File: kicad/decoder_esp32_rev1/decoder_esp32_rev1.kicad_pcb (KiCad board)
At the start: 2 copper layers, 75.9 x 42 mm, 53 parts, among them J1 TRCK_IN, J2 F_2, J3 F_3, J4 F_1, J5 F_4, J6 AUX_5V, J8 MTR_OUT, J9 to_cap_brd, Q1 BSS138, Q2 BSS138, Q3 BSS138, Q4 BSS138, U1 ESP32-C3_SUPERMINI_TH, U2 LM2596S-5, U3 TB67H450FNG_EL

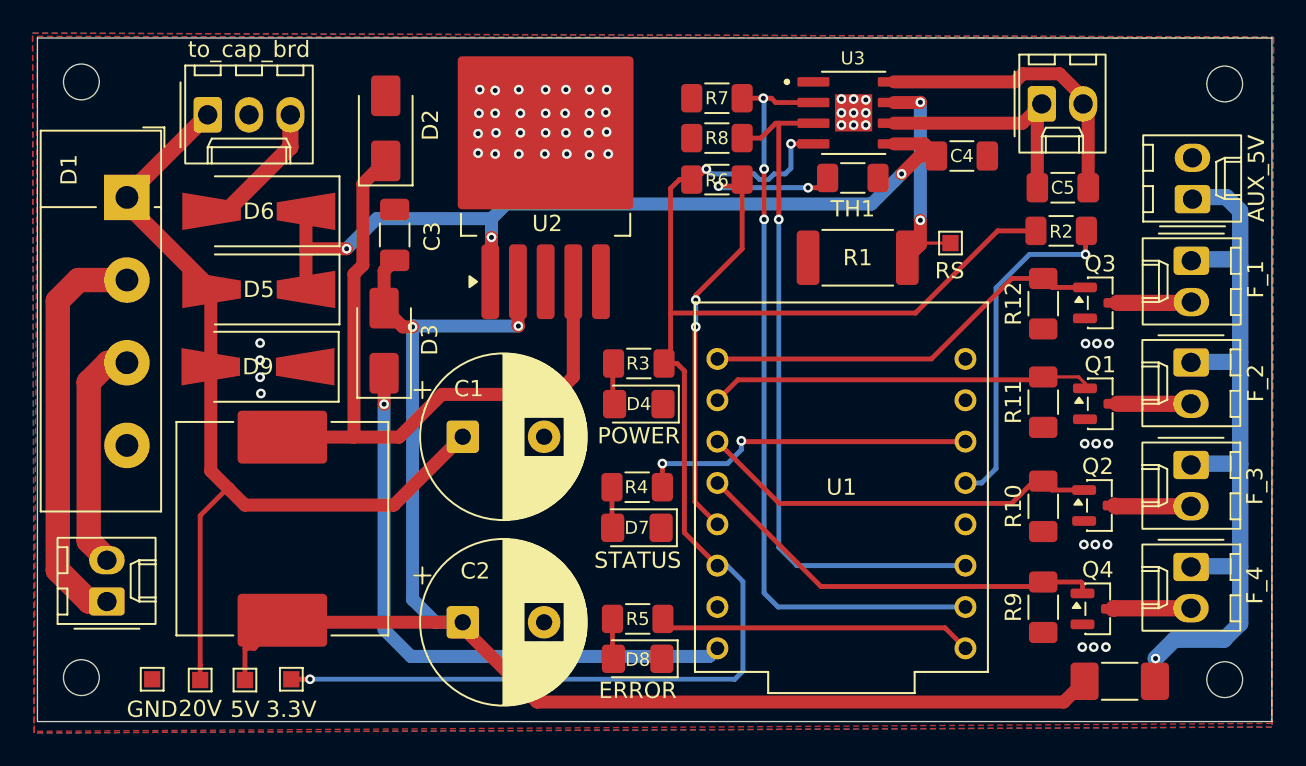
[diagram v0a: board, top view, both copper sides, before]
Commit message: KiCad rev3: schematic/PCB layout reorganization + remove PWR_FLAG symbols
Reordered components and wiring for better schematic overview.
Removed #FLG01/#FLG02 PWR_FLAG symbols (cosmetic ERC cleanup).
No netlist or component value changes.

Co-Authored-By: Claude Sonnet 4.6 <noreply@anthropic.com>
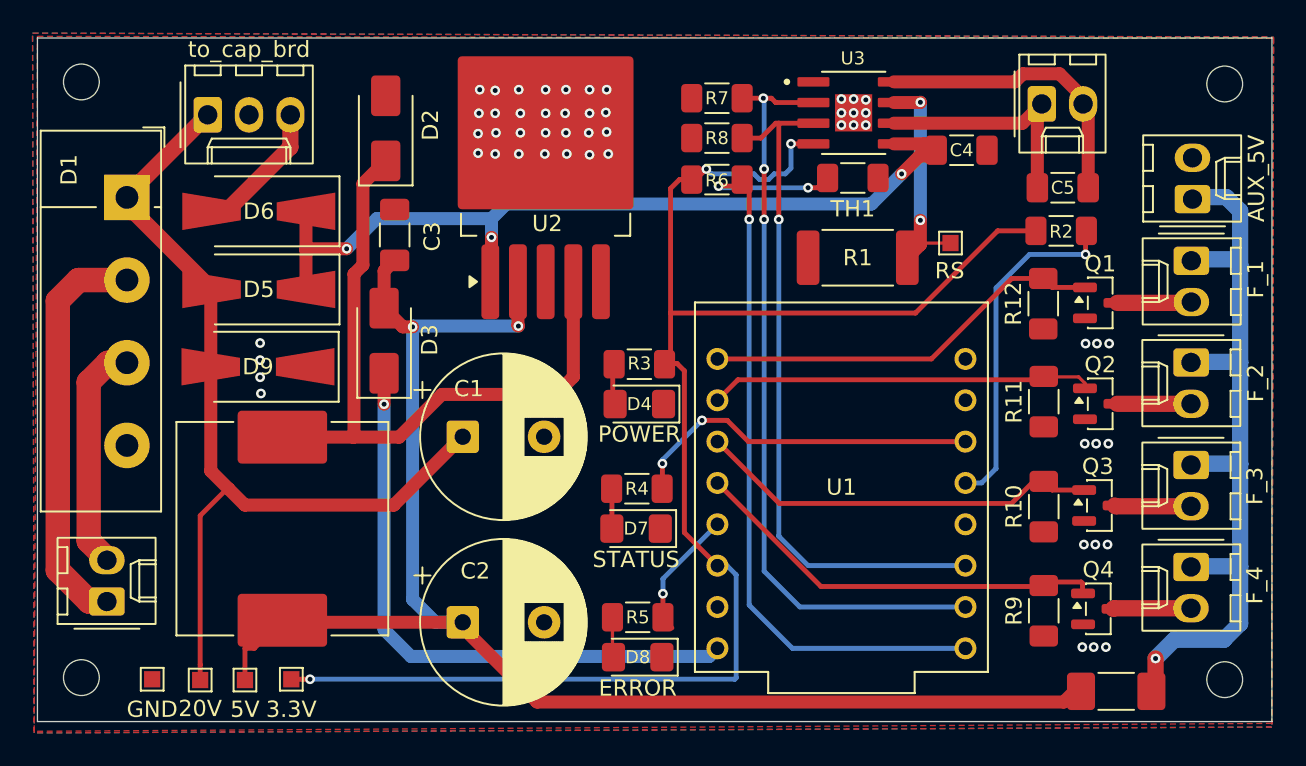
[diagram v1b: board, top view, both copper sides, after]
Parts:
- C1: value 470uF - 35V -> ~
- moved F1 0.66 mm to (116.3, 148.2), turned to 0 degrees
- moved C4 0.36 mm to (106.8, 114.9)
- moved R9 0.22 mm to (111.8, 143.2)
- moved D8 0.10 mm to (86.9, 146.1)
- moved R5 0.10 mm to (86.9, 143.6)
- moved R4 0.10 mm to (86.8, 135.7)
- moved D7 0.07 mm to (86.8, 138.2)
- moved R3 0.05 mm to (87.0, 128.1)
- renumbered Q3 to Q1, Q1 to Q2, Q2 to Q3, TP3 to TP2, TP2 to TP3
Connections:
- F1 pad 1: Net-(J2-Pin_1) -> Net-(D3-A)
- F1 pad 2: Net-(D3-A) -> Net-(J2-Pin_1)
- R5 pad 1: Net-(U1-GPIO5) -> Net-(U1-GPIO4)
- R6 pad 2: Net-(U1-GPIO4) -> Net-(U1-GPIO5)
- TH1 pad 1: Net-(U1-GPIO4) -> Net-(U1-GPIO5)
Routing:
- net Net-(U1-GPIO5): track 19.3 -> 49.3 mm, vias 0 -> 3
- net Net-(U1-GPIO4): track 31.6 -> 7.88 mm, vias 4 -> 1
- net Net-(J2-Pin_1): track 43.0 -> 45.2 mm
- net Net-(U1-GPIO10): track 21.0 -> 21.8 mm
- net Net-(U1-GPIO6): track 47.6 -> 46.9 mm

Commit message: Fix GPIO4/GPIO5 assignment: thermistor back on GPIO4 (ADC1_CH4)
GPIO5 has no ADC capability on ESP32-C3 — thermistor must stay on
GPIO4 (ADC1_CH4). Swap ERROR LED to GPIO5 (digital output only).

Co-Authored-By: Claude Sonnet 4.6 <noreply@anthropic.com>
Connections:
- R5 pad 1: Net-(U1-GPIO4) -> Net-(U1-GPIO5)
- R6 pad 2: Net-(U1-GPIO5) -> Net-(U1-GPIO4)
- TH1 pad 1: Net-(U1-GPIO5) -> Net-(U1-GPIO4)
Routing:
- net Net-(U1-GPIO5): track 49.3 -> 19.4 mm, vias 3 -> 0
- net Net-(U1-GPIO4): track 7.88 -> 31.0 mm, vias 1 -> 3
